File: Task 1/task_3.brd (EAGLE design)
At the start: 100 x 100 mm, 6 parts

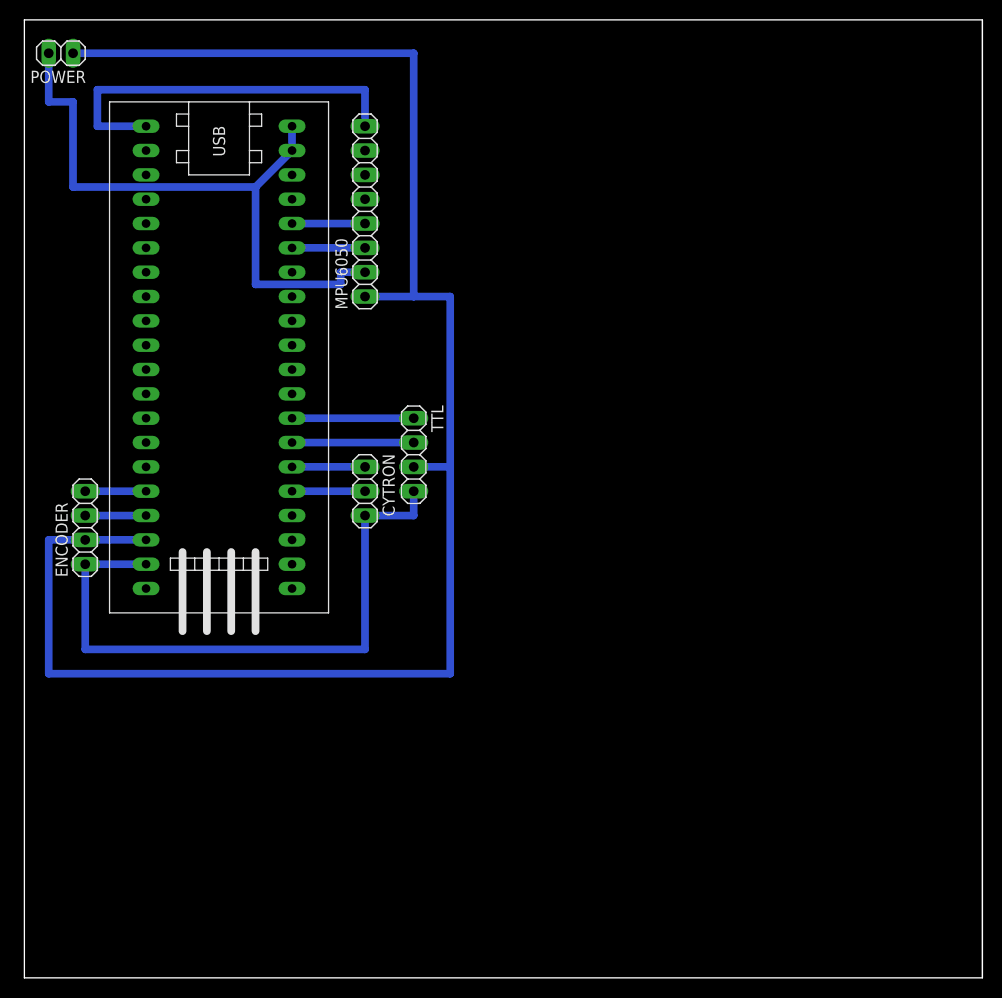
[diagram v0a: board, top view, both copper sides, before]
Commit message: added second ttl and used correct data pinheads
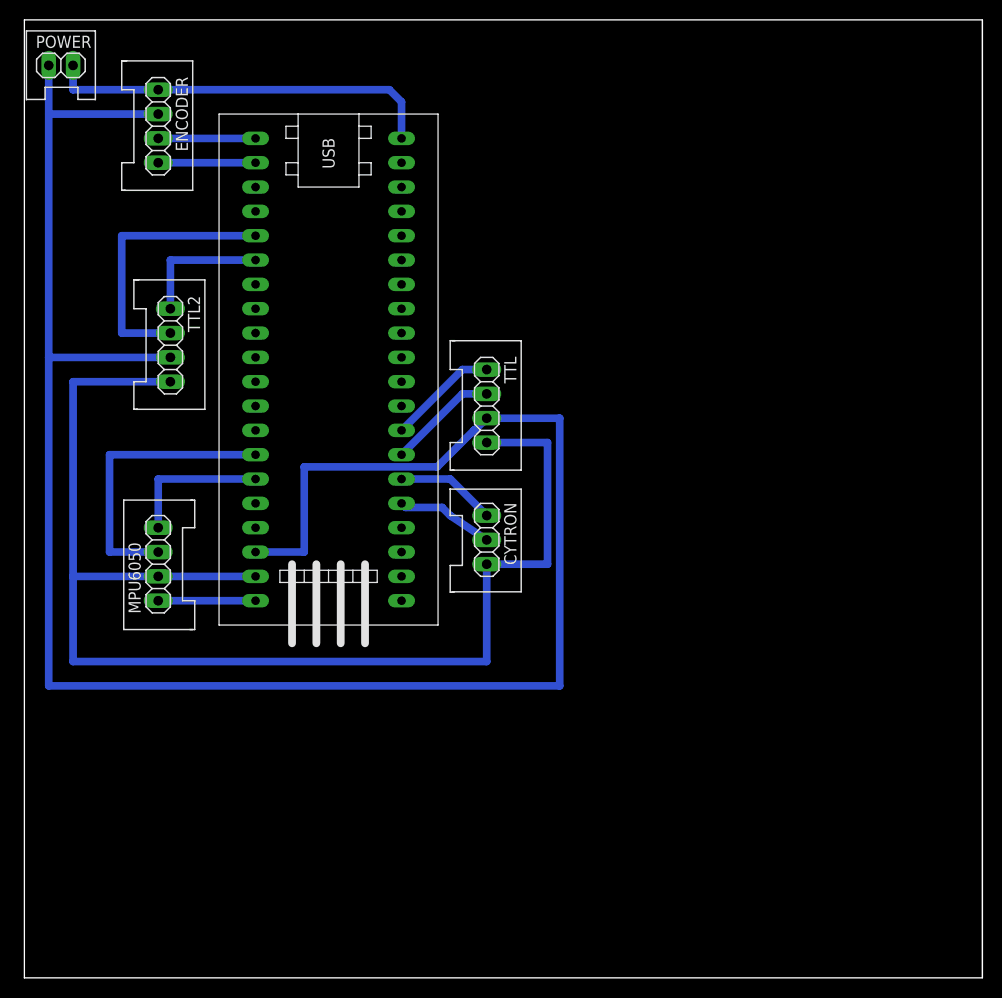
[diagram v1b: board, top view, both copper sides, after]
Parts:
- added TTL2: (no value), MIA_LIBRARY-2-2-2:1X04_DATA
- CYTRON: device MIA_LIBRARY-2-2-2:1X03 -> MIA_LIBRARY-2-2-2:1X03_DATA
- ENCODER, TTL: device MIA_LIBRARY-2-2-2:1X04 -> MIA_LIBRARY-2-2-2:1X04_DATA
- MPU6050: device MIA_LIBRARY-2-2-2:1X08 -> MIA_LIBRARY-2-2-2:1X04_DATA
- POWER: device MIA_LIBRARY-2-2-2:1X02 -> MIA_LIBRARY-2-2-2:1X02_DATA
- moved MPU6050 42.7 mm to (14.0, 43.2)
- moved ENCODER 42.6 mm to (14.0, 88.9), turned to 270 degrees
- moved CYTRON 13.7 mm to (48.3, 45.7)
- moved U$1 11.5 mm to (31.8, 64.8)
- moved TTL 9.16 mm to (48.3, 59.7)
- moved POWER 1.27 mm to (3.81, 95.2), turned to 0 degrees
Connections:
- new net GND2: ENCODER.1, POWER.2, U$1.GND_3
- net 3.3V@1: now also MPU6050.1
- net 5V: now also TTL2.3; no longer MPU6050.1
- net GND: now also MPU6050.2, TTL2.4; no longer ENCODER.1
- net GND1: no longer MPU6050.2, POWER.2, U$1.GND_3
- net PA_8: now also TTL2.2
- net PA_9: now also TTL2.1
- net PB_10: no longer MPU6050.3
- net PB_11: no longer MPU6050.4
- net PB_12: now also ENCODER.3; no longer MPU6050.8
- net PB_13: now also ENCODER.4
- net PB_6: now also MPU6050.3
- net PB_7: now also MPU6050.4
- net PB_8: no longer ENCODER.4
- net PB_9: no longer ENCODER.3
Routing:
- net GND: track 66.0 -> 137.2 mm
- net GND1: track 66.3 -> 0.00 mm
- net GND2: track 0.00 -> 41.2 mm
- net 5V: track 179.1 -> 212.9 mm
- net PB_6: track 0.00 -> 30.5 mm
- net PB_12: track 40.6 -> 10.2 mm
- net PA_8: track 0.00 -> 29.2 mm
- net PB_7: track 0.00 -> 15.2 mm
- net PA_9: track 0.00 -> 14.0 mm
- net PB_13: track 0.00 -> 10.2 mm
- net 3.3V@1: track 0.00 -> 10.2 mm
- net PB_11: track 7.62 -> 0.00 mm
- net PB_10: track 7.62 -> 0.00 mm
- net PB_9: track 6.35 -> 0.00 mm
- net PB_8: track 6.35 -> 0.00 mm
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
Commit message: fixed pin configuration and routing errors, and also updated dimensions and added vias
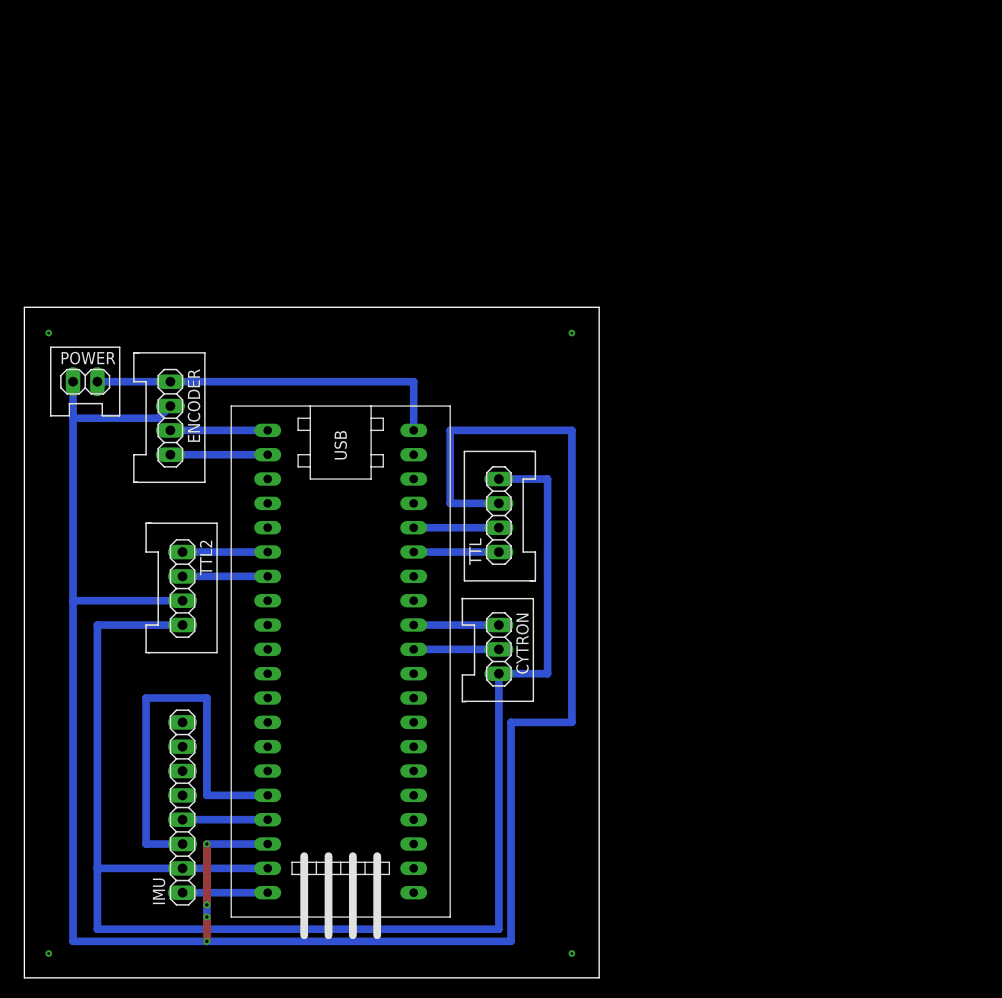
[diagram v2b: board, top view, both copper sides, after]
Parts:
- removed MPU6050: (no value), MIA_LIBRARY-2-2-2:1X04_DATA
- added IMU: (no value), MIA_LIBRARY-2-2-2:1X08
- moved POWER 33.1 mm to (6.35, 62.2)
- moved ENCODER 30.5 mm to (15.2, 58.4)
- moved U$1 30.5 mm to (33.0, 34.3)
- moved TTL2 25.4 mm to (16.5, 40.6)
- moved CYTRON 11.5 mm to (49.5, 34.3)
- moved TTL 11.5 mm to (49.5, 48.3), turned to 90 degrees
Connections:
- net 3.3V@1: now also IMU.1; no longer MPU6050.1
- net GND: now also IMU.2; no longer MPU6050.2
- net PA_0: no longer CYTRON.2
- net PA_1: no longer CYTRON.1
- net PA_10: now also TTL2.2
- net PA_2: no longer TTL.2
- net PA_3: no longer TTL.1
- net PA_6: now also CYTRON.2
- net PA_7: now also CYTRON.1
- net PA_8: no longer TTL2.2
- net PB_10: now also TTL.1
- net PB_11: now also TTL.2
- net PB_6: no longer MPU6050.3
- net PB_7: no longer MPU6050.4
- net PB_8: now also IMU.3
- net PB_9: now also IMU.4
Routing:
- net PB_8: track 0.00 -> 41.9 mm
- net PB_6: track 30.5 -> 0.00 mm
- net PA_8: track 29.2 -> 0.00 mm
- net GND: track 137.2 -> 157.5 mm
- net PB_7: track 15.2 -> 0.00 mm
- net 5V: track 212.9 -> 227.9 mm, vias 0 -> 4
- net PA_3: track 11.5 -> 0.00 mm
- net PA_2: track 11.5 -> 0.00 mm
- net PA_1: track 10.5 -> 0.00 mm
- net PA_0: track 10.2 -> 0.00 mm
- net PB_11: track 0.00 -> 8.89 mm
- net PB_10: track 0.00 -> 8.89 mm
- net PA_7: track 0.00 -> 8.89 mm
- net PA_6: track 0.00 -> 8.89 mm
- net PB_9: track 0.00 -> 8.89 mm
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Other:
- board size 100 x 100 mm -> 60 x 70 mm

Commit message: fixed minor error
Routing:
- net 5V: track 227.9 -> 225.3 mm, vias 4 -> 2
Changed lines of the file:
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@@
 <wire x1="49.53" y1="49.53" x2="44.45" y2="49.53" width="0.8" layer="16"/>
 <wire x1="44.45" y1="49.53" x2="44.45" y2="57.15" width="0.8" layer="16"/>
-<wire x1="5.08" y1="3.81" x2="5.08" y2="39.37" width="0.8" layer="16"/>
+<wire x1="5.08" y1="6.35" x2="5.08" y2="39.37" width="0.8" layer="16"/>
 <wire x1="57.15" y1="57.15" x2="57.15" y2="26.67" width="0.8" layer="16"/>
 <wire x1="57.15" y1="26.67" x2="50.8" y2="26.67" width="0.8" layer="16"/>
 <wire x1="50.8" y1="26.67" x2="50.8" y2="3.81" width="0.8" layer="16"/>
 <wire x1="50.8" y1="3.81" x2="19.05" y2="3.81" width="0.8" layer="16"/>
-<wire x1="19.05" y1="3.81" x2="5.08" y2="3.81" width="0.8" layer="16"/>
+<wire x1="19.05" y1="3.81" x2="19.05" y2="6.35" width="0.8" layer="16"/>
+<wire x1="19.05" y1="6.35" x2="5.08" y2="6.35" width="0.8" layer="16"/>
 <wire x1="44.45" y1="57.15" x2="57.15" y2="57.15" width="0.8" layer="16"/>
-<via x="19.05" y="3.81" extent="1-16" drill="0.35"/>
-<wire x1="19.05" y1="3.81" x2="19.05" y2="6.35" width="0.8" layer="1"/>
 <via x="19.05" y="6.35" extent="1-16" drill="0.35"/>
-<wire x1="19.05" y1="6.35" x2="19.05" y2="7.62" width="0.8" layer="16"/>
-<via x="19.05" y="7.62" extent="1-16" drill="0.35"/>
-<wire x1="19.05" y1="7.62" x2="19.05" y2="13.97" width="0.8" layer="1"/>
+<wire x1="19.05" y1="6.35" x2="19.05" y2="13.97" width="0.8" layer="1"/>
 <via x="19.05" y="13.97" extent="1-16" drill="0.35"/>
 <wire x1="19.05" y1="13.97" x2="25.4" y2="13.97" width="0.8" layer="16"/>
@@
 <wire x1="16.51" y1="36.83" x2="7.62" y2="36.83" width="0.8" layer="16"/>
 <wire x1="7.62" y1="36.83" x2="7.62" y2="11.43" width="0.8" layer="16"/>
-<wire x1="7.62" y1="11.43" x2="7.62" y2="5.08" width="0.8" layer="16"/>
+<wire x1="7.62" y1="11.43" x2="7.62" y2="7.62" width="0.8" layer="16"/>
 <wire x1="49.53" y1="31.75" x2="49.53" y2="5.08" width="0.8" layer="16"/>
-<wire x1="49.53" y1="5.08" x2="7.62" y2="5.08" width="0.8" layer="16"/>
+<wire x1="49.53" y1="5.08" x2="20.32" y2="5.08" width="0.8" layer="16"/>
+<wire x1="20.32" y1="5.08" x2="20.32" y2="7.62" width="0.8" layer="16"/>
+<wire x1="20.32" y1="7.62" x2="7.62" y2="7.62" width="0.8" layer="16"/>
 <contactref element="IMU" pad="2"/>
 <contactref element="TTL" pad="4"/>

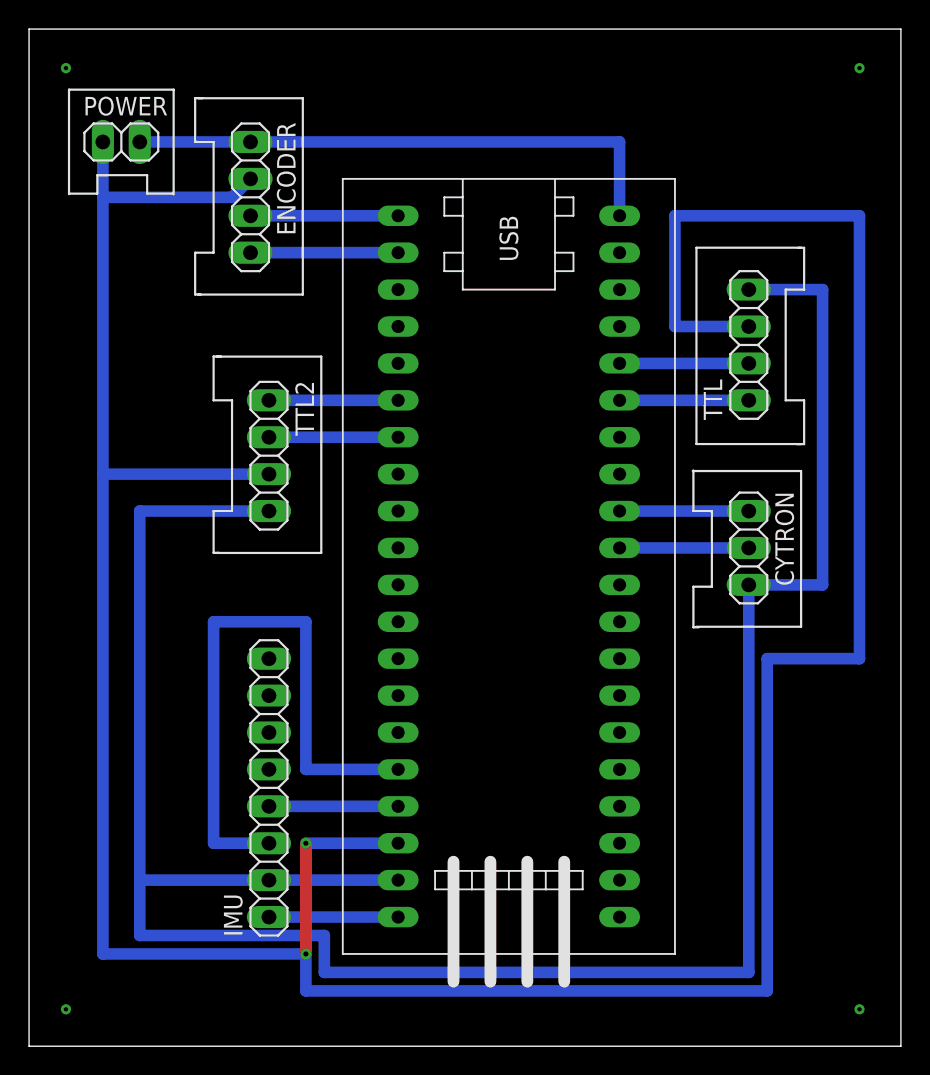
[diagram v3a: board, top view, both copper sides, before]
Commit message: ommitted use of jumpers
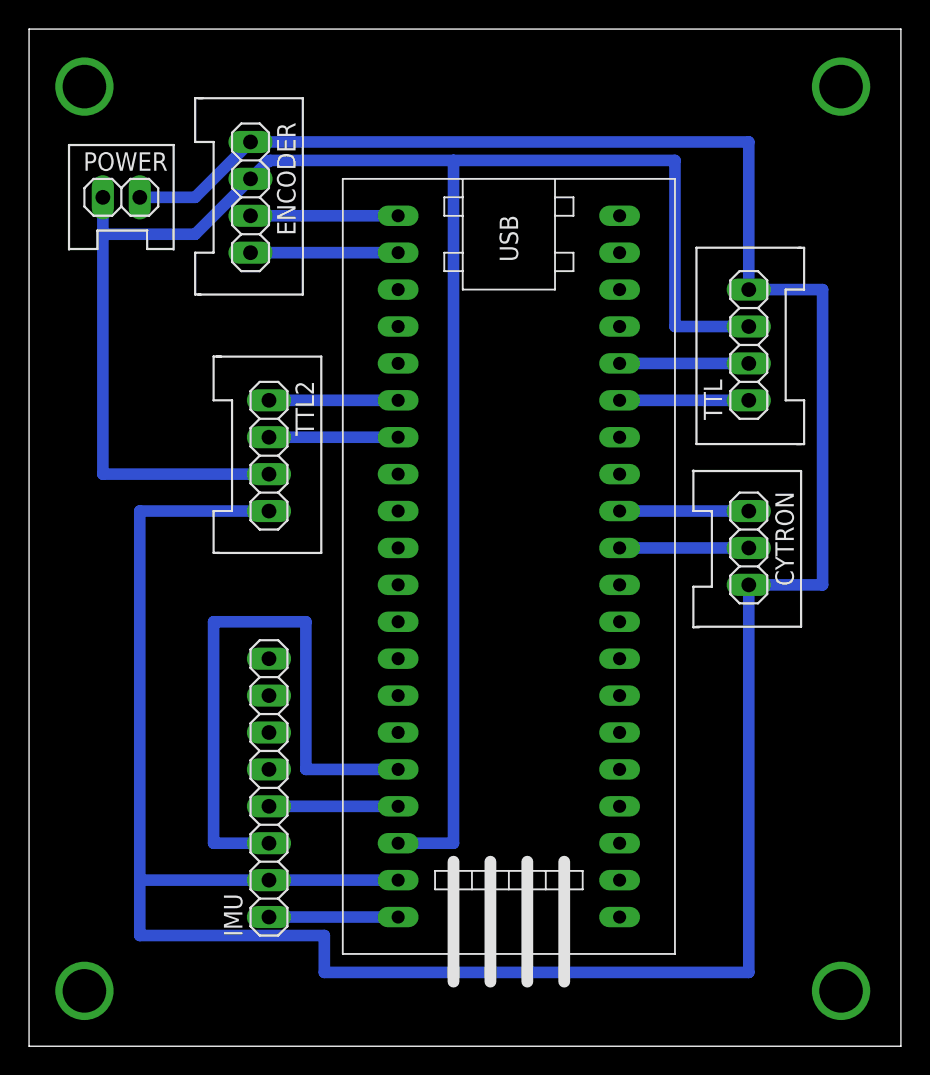
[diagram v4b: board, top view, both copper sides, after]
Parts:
- moved POWER 3.81 mm to (6.35, 58.4)
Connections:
- net GND: now also ENCODER.1, POWER.2
- net GND2: no longer ENCODER.1, POWER.2
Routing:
- net 5V: track 225.3 -> 139.3 mm, vias 2 -> 0
- net GND: track 157.5 -> 211.1 mm
- net GND2: track 38.1 -> 0.00 mm
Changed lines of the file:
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@@
 </element>
 <element name="U$1" library="MIA_LIBRARY-2-2-2" library_urn="urn:adsk.eagle:library:16672108" package="STM32F103C8T6-MODULE" package3d_urn="urn:adsk.eagle:package:15814189/2" value="STM32F103C8T6-MODULE" x="33.02" y="34.29" smashed="yes" rot="R270"/>
-<element name="POWER" library="MIA_LIBRARY-2-2-2" library_urn="urn:adsk.eagle:library:16672108" package="1X02_DATA" package3d_urn="urn:adsk.eagle:package:15814197/4" value="" x="6.35" y="62.23" smashed="yes">
-<attribute name="NAME" x="3.7338" y="64.0588" size="1.27" layer="25" ratio="10"/>
-<attribute name="VALUE" x="3.81" y="59.055" size="1.27" layer="27"/>
+<element name="POWER" library="MIA_LIBRARY-2-2-2" library_urn="urn:adsk.eagle:library:16672108" package="1X02_DATA" package3d_urn="urn:adsk.eagle:package:15814197/4" value="" x="6.35" y="58.42" smashed="yes">
+<attribute name="NAME" x="3.7338" y="60.2488" size="1.27" layer="25" ratio="10"/>
+<attribute name="VALUE" x="3.81" y="55.245" size="1.27" layer="27"/>
 </element>
 <element name="TTL2" library="MIA_LIBRARY-2-2-2" library_urn="urn:adsk.eagle:library:16672108" package="1X04_DATA" package3d_urn="urn:adsk.eagle:package:15814199/5" value="" x="16.51" y="40.64" smashed="yes" rot="R270">
@@
 <contactref element="ENCODER" pad="2"/>
 <contactref element="POWER" pad="1"/>
-<wire x1="5.08" y1="62.23" x2="5.08" y2="58.42" width="0.8" layer="16"/>
-<wire x1="5.08" y1="58.42" x2="5.08" y2="39.37" width="0.8" layer="16"/>
+<wire x1="5.08" y1="58.42" x2="5.08" y2="55.88" width="0.8" layer="16"/>
+<wire x1="5.08" y1="55.88" x2="5.08" y2="39.37" width="0.8" layer="16"/>
 <contactref element="TTL2" pad="3"/>
-<wire x1="15.24" y1="59.69" x2="13.97" y2="58.42" width="0.8" layer="16"/>
-<wire x1="13.97" y1="58.42" x2="5.08" y2="58.42" width="0.8" layer="16"/>
+<wire x1="15.24" y1="59.69" x2="11.43" y2="55.88" width="0.8" layer="16"/>
+<wire x1="11.43" y1="55.88" x2="5.08" y2="55.88" width="0.8" layer="16"/>
 <wire x1="16.51" y1="39.37" x2="5.08" y2="39.37" width="0.8" layer="16"/>
 <wire x1="49.53" y1="49.53" x2="44.45" y2="49.53" width="0.8" layer="16"/>
-<wire x1="44.45" y1="49.53" x2="44.45" y2="57.15" width="0.8" layer="16"/>
-<wire x1="5.08" y1="6.35" x2="5.08" y2="39.37" width="0.8" layer="16"/>
-<wire x1="57.15" y1="57.15" x2="57.15" y2="26.67" width="0.8" layer="16"/>
-<wire x1="57.15" y1="26.67" x2="50.8" y2="26.67" width="0.8" layer="16"/>
-<wire x1="50.8" y1="26.67" x2="50.8" y2="3.81" width="0.8" layer="16"/>
-<wire x1="50.8" y1="3.81" x2="19.05" y2="3.81" width="0.8" layer="16"/>
-<wire x1="19.05" y1="3.81" x2="19.05" y2="6.35" width="0.8" layer="16"/>
-<wire x1="19.05" y1="6.35" x2="5.08" y2="6.35" width="0.8" layer="16"/>
-<wire x1="44.45" y1="57.15" x2="57.15" y2="57.15" width="0.8" layer="16"/>
-<via x="19.05" y="6.35" extent="1-16" drill="0.35"/>
-<wire x1="19.05" y1="6.35" x2="19.05" y2="13.97" width="0.8" layer="1"/>
-<via x="19.05" y="13.97" extent="1-16" drill="0.35"/>
-<wire x1="19.05" y1="13.97" x2="25.4" y2="13.97" width="0.8" layer="16"/>
+<wire x1="44.45" y1="60.96" x2="29.21" y2="60.96" width="0.8" layer="16"/>
+<wire x1="29.21" y1="60.96" x2="29.21" y2="13.97" width="0.8" layer="16"/>
+<wire x1="29.21" y1="13.97" x2="25.4" y2="13.97" width="0.8" layer="16"/>
+<wire x1="44.45" y1="49.53" x2="44.45" y2="60.96" width="0.8" layer="16"/>
+<wire x1="15.24" y1="59.69" x2="16.4656" y2="60.9156" width="0.8" layer="16"/>
+<wire x1="16.4656" y1="60.9156" x2="16.54644375" y2="60.9156" width="0.8" layer="16"/>
+<wire x1="16.54644375" y1="60.9156" x2="16.59084375" y2="60.96" width="0.8" layer="16"/>
+<wire x1="16.59084375" y1="60.96" x2="29.21" y2="60.96" width="0.8" layer="16"/>
 </signal>
 <signal name="3.3V@1">
@@
 <wire x1="16.51" y1="11.43" x2="25.4" y2="11.43" width="0.8" layer="16"/>
 <wire x1="16.51" y1="11.43" x2="7.62" y2="11.43" width="0.8" layer="16"/>
+<contactref element="POWER" pad="2"/>
+<contactref element="ENCODER" pad="1"/>
+<wire x1="11.43" y1="58.42" x2="15.24" y2="62.23" width="0.8" layer="16"/>
+<wire x1="11.43" y1="58.42" x2="7.62" y2="58.42" width="0.8" layer="16"/>
+<wire x1="15.24" y1="62.23" x2="49.53" y2="62.23" width="0.8" layer="16"/>
+<wire x1="49.53" y1="62.23" x2="49.53" y2="52.07" width="0.8" layer="16"/>
 </signal>
 <signal name="GND1">
@@
 <signal name="GND2">
 <contactref element="U$1" pad="GND_3"/>
-<contactref element="ENCODER" pad="1"/>
-<contactref element="POWER" pad="2"/>
-<wire x1="7.62" y1="62.23" x2="15.24" y2="62.23" width="0.8" layer="16"/>
-<wire x1="15.24" y1="62.23" x2="40.64" y2="62.23" width="0.8" layer="16"/>
-<wire x1="40.64" y1="62.23" x2="40.64" y2="57.15" width="0.8" layer="16"/>
 </signal>
 <signal name="N$3">
-<via x="2.54" y="2.54" extent="1-16" drill="0.3"/>
+<via x="3.81" y="3.81" extent="1-16" drill="3"/>
 </signal>
 <signal name="N$4">
-<via x="57.15" y="2.54" extent="1-16" drill="0.3"/>
+<via x="55.88" y="3.81" extent="1-16" drill="3"/>
 </signal>
 <signal name="N$5">
-<via x="57.15" y="67.31" extent="1-16" drill="0.3"/>
+<via x="55.88" y="66.04" extent="1-16" drill="3"/>
 </signal>
 <signal name="N$6">
-<via x="2.54" y="67.31" extent="1-16" drill="0.3"/>
+<via x="3.81" y="66.04" extent="1-16" drill="3"/>
 </signal>
 </signals>
